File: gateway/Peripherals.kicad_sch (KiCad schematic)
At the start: 29 parts, among them IC1501 ATECC608B-SSHDA, IC1502 TUSB320, IC1503 TXS0108EPW, IC1504 TXS0102DCU, IC1505 TXB0102DCU, IC1506 TXS0102DCU, X1501 OTG, X1502 GPIO, X1503 I2C, X1504 CAN, X1505 I2C

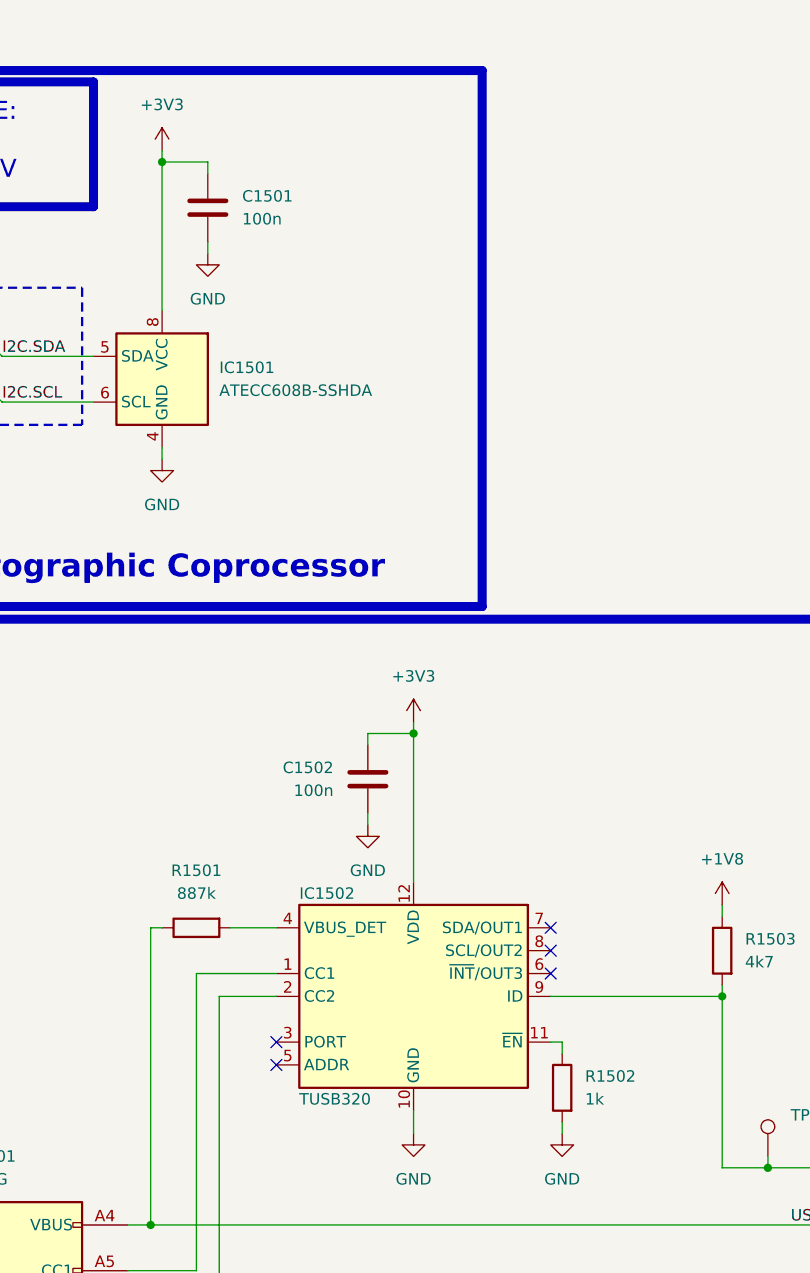
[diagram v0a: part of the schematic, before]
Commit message: Improving Thread
- Add boot signal for Thread MCU
- Add debug LED for nRF5340
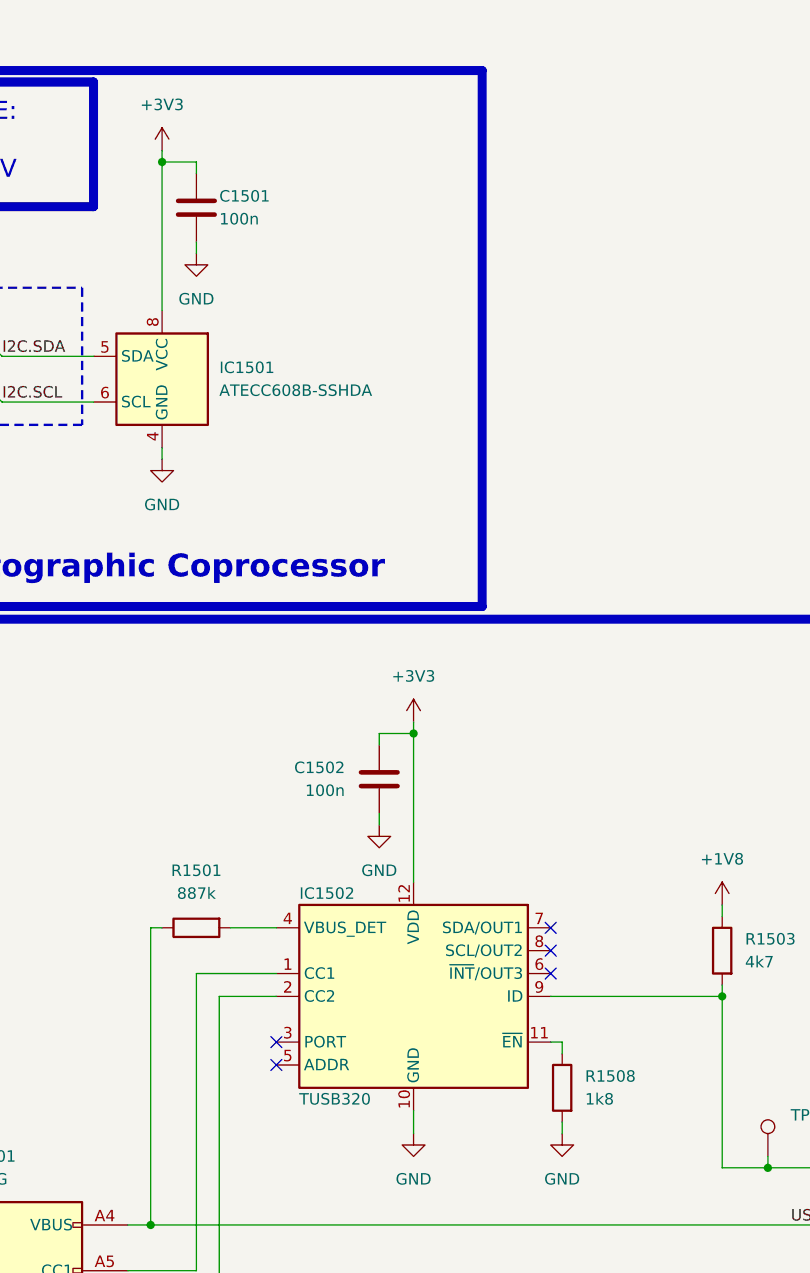
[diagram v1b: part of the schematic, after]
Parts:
- removed R1502: 1k, Resistor_SMD:R_0805_2012Metric, symbol Device:R
- added R1508: 1k8, Resistor_SMD:R_0805_2012Metric, symbol Device:R
- TP1501: value ~ -> (none)
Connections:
- net GND: now also R1508.2
- net at IC1502.11 (~{EN}): now also R1508.1
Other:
- moved on the sheet: C1501, C1502

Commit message: Working on PCB
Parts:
- TP1501: value (none) -> ~
- X1502: footprint Connector_Phoenix_MSTB:PhoenixContact_MSTBA_2,5_10-G-5,08_1x10_P5.08mm_Horizontal -> Phoenix:MSTBA_2,5_10-G-5,08_1x10_P5.08mm_Horizontal; mouser# 51-1757323 -> 651-1757323
- X1503, X1504, X1505: footprint Connector_Phoenix_MSTB:PhoenixContact_MSTBA_2,5_4-G-5,08_1x04_P5.08mm_Horizontal -> Phoenix:MSTBA_2,5_4-G-5,08_1x04_P5.08mm_Horizontal
- renumbered R1508 to R1502
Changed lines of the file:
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@@
 			)
 		)
-		(property "Footprint" "Connector_Phoenix_MSTB:PhoenixContact_MSTBA_2,5_10-G-5,08_1x10_P5.08mm_Horizontal"
+		(property "Footprint" "Phoenix:MSTBA_2,5_10-G-5,08_1x10_P5.08mm_Horizontal"
 			(at 281.94 193.04 0)
 			(hide yes)
@@
 			)
 		)
-		(property "mouser#" "51-1757323"
+		(property "mouser#" "651-1757323"
 			(at 281.94 193.04 0)
 			(hide yes)
@@
 			)
 		)
-		(property "Footprint" "Connector_Phoenix_MSTB:PhoenixContact_MSTBA_2,5_4-G-5,08_1x04_P5.08mm_Horizontal"
+		(property "Footprint" "Phoenix:MSTBA_2,5_4-G-5,08_1x04_P5.08mm_Horizontal"
 			(at 391.16 151.13 0)
 			(hide yes)
@@
 			)
 		)
-		(property "Value" ""
+		(property "Value" "~"
 			(at 123.19 216.4079 0)
 			(show_name no)
@@
 			)
 		)
-		(property "Footprint" "Connector_Phoenix_MSTB:PhoenixContact_MSTBA_2,5_4-G-5,08_1x04_P5.08mm_Horizontal"
+		(property "Footprint" "Phoenix:MSTBA_2,5_4-G-5,08_1x04_P5.08mm_Horizontal"
 			(at 391.16 209.55 0)
 			(hide yes)
@@
 			)
 		)
-		(property "Footprint" "Connector_Phoenix_MSTB:PhoenixContact_MSTBA_2,5_4-G-5,08_1x04_P5.08mm_Horizontal"
+		(property "Footprint" "Phoenix:MSTBA_2,5_4-G-5,08_1x04_P5.08mm_Horizontal"
 			(at 391.16 93.98 0)
 			(hide yes)
@@
 		(in_pos_files yes)
 		(dnp no)
-		(property "Reference" "R1508"
+		(property "Reference" "R1502"
 			(at 100.33 209.5499 0)
 			(show_name no)
@@
 			(project "Gateway"
 				(path "/d5742f03-3b1a-42e5-a384-018bd4b919aa/c5103ceb-5325-4a84-a025-9638a412984e/80a97db3-ff4e-4b40-a5b0-8dd5c51e4d83"
-					(reference "R1508")
+					(reference "R1502")
 					(unit 1)
 				)

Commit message: Working on layout
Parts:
- C1501, IC1501, R1504, R1505, R1506, R1507: now not fitted; now left out of the parts list
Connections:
- net +3V3: no longer C1504.1, C1508.1, C1509.1, C1510.1, IC1503.19 (VCCB), IC1504.7 (VCCB), IC1505.7 (VCCB), IC1506.7 (VCCB), R1504.1, R1505.1, R1506.1, R1507.1, X1502.1 (Pin_1), X1503.1 (Pin_1), X1504.1 (Pin_1), X1505.1 (Pin_1)
- net SCL_{HV}: no longer names the net of IC1504.1 (B2), R1506.2, X1503.3 (Pin_3)
- net SDA_{HV}: no longer names the net of IC1504.8 (B1), R1504.2, X1503.2 (Pin_2)
- new net: C1504.1, IC1503.19 (VCCB), X1502.1 (Pin_1)
- new net: C1509.1, IC1505.7 (VCCB), X1504.1 (Pin_1)
- new net: C1508.1, IC1504.7 (VCCB), R1504.1, R1506.1, X1503.1 (Pin_1)
- new net: C1510.1, IC1506.7 (VCCB), R1505.1, R1507.1, X1505.1 (Pin_1)
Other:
- moved on the sheet: C1505, C1507, C1508, C1510, IC1504, IC1506, X1503, X1505

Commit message: Working on revision 1.0.0
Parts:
- C1501: symbol Device:C -> partdb:08055C104K4Z4A; Category (none) -> Kondensator/MLCC; MPN (none) -> 08055C104K4Z4A; Manufacturer (none) -> KYOCERA AVX; Manufacturing Status (none) -> Active; Mass (none) -> 0.006 g; Mouser SPN (none) -> 581-08055C104K4Z4A; Part-DB Footprint (none) -> 0805; Part-DB ID (none) -> 109; Part-DB URL (none) -> https://inventory.lan/de/part/109/info; Stock (none) -> 6; Storage Location (none) -> Sortierregal; manf# 08053C104M4T4A -> 08055C104K4Z4A; mouser# 581-08053C104M4T4A -> 581-08055C104K4Z4A; now in the parts list
- C1502, C1503, C1504, C1505, C1506, C1507, C1508, C1509, C1510: symbol Device:C -> partdb:08055C104K4Z4A; Category (none) -> Kondensator/MLCC; MPN (none) -> 08055C104K4Z4A; Manufacturer (none) -> KYOCERA AVX; Manufacturing Status (none) -> Active; Mass (none) -> 0.006 g; Mouser SPN (none) -> 581-08055C104K4Z4A; Part-DB Footprint (none) -> 0805; Part-DB ID (none) -> 109; Part-DB URL (none) -> https://inventory.lan/de/part/109/info; Stock (none) -> 6; Storage Location (none) -> Sortierregal; manf# 08053C104M4T4A -> 08055C104K4Z4A; mouser# 581-08053C104M4T4A -> 581-08055C104K4Z4A
- R1502: symbol Device:R -> partdb:CR0805-JW-182ELF; Category (none) -> Widerstand/Dickfilmwiderstand; MPN (none) -> CR0805-JW-182ELF; Manufacturer (none) -> Bourns; Manufacturing Status (none) -> Active; Mass (none) -> 0.0055 g; Mouser SPN (none) -> 652-CR0805JW-182ELF; Part-DB Footprint (none) -> 0805; Part-DB ID (none) -> 350; Part-DB URL (none) -> https://inventory.lan/de/part/350/info; Stock (none) -> 0; manf# CR0805-FX-1801GLF -> CR0805-JW-182ELF; mouser# 652-CR0805-FX-1801GLF -> 652-CR0805JW-182ELF
- R1503: symbol Device:R -> partdb:CR0805-JW-472ELF; Category (none) -> Widerstand/Dickfilmwiderstand; MPN (none) -> CR0805-JW-472ELF; Manufacturer (none) -> Bourns; Manufacturing Status (none) -> Active; Mass (none) -> 0.006 g; Mouser SPN (none) -> 652-CR0805JW-472ELF; Part-DB Footprint (none) -> 0805; Part-DB ID (none) -> 78; Part-DB URL (none) -> https://inventory.lan/de/part/78/info; Stock (none) -> 50; Storage Location (none) -> Sortierregal; mouser# 652-CR0805-JW-472ELF -> 652-CR0805JW-472ELF
- R1504, R1505, R1506, R1507: symbol Device:R -> partdb:CR0805-JW-332ELF; Category (none) -> Widerstand/Dickfilmwiderstand; MPN (none) -> CR0805-JW-332ELF; Manufacturer (none) -> Bourns; Manufacturing Status (none) -> Active; Mass (none) -> 0.006 g; Mouser SPN (none) -> 652-CR0805-JW-332ELF; Part-DB Footprint (none) -> 0805; Part-DB ID (none) -> 79; Part-DB URL (none) -> https://inventory.lan/de/part/79/info; Stock (none) -> 50; Storage Location (none) -> Sortierregal; manf# CR0805-FX-3301GLF -> CR0805-JW-332ELF; mouser# 652-CR0805-FX-3301GLF -> 652-CR0805-JW-332ELF
